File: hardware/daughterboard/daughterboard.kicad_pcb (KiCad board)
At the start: 4 copper layers, 51.1 x 51 mm, 88 parts, among them J1 Custom_PCIe_x4, U0 XTR200, U1 XTR200, U10 REF5030EIDR, U11 AD7193, U2 XTR200, U20 DAC80508Z, U3 XTR200, U4 XTR200, U5 XTR200, U6 XTR200, U7 XTR200, U8 SN74LV165

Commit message: add board
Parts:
- added FID1: Fiducial, Fiducial:Fiducial_1mm_Mask2mm, F.Cu at (101.6, 67.0)
- added FID2: Fiducial, Fiducial:Fiducial_1mm_Mask2mm, F.Cu at (149.6, 106.5)
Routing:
- net GND: vias 188 -> 193
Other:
- board text added: "KOI 8X8"
- board text removed: "OQ V1"

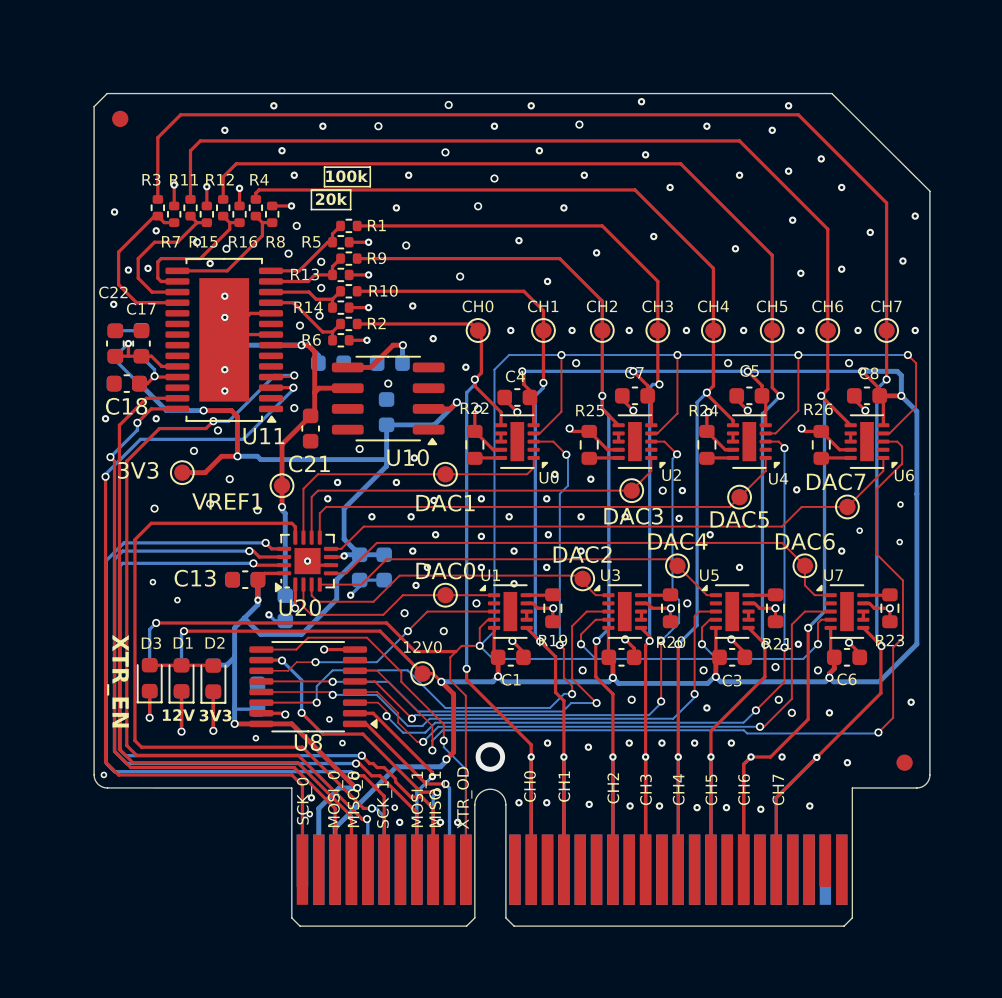
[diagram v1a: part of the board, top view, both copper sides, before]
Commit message: updated daughterboard with eeprom and some layout improvements and padne simulations
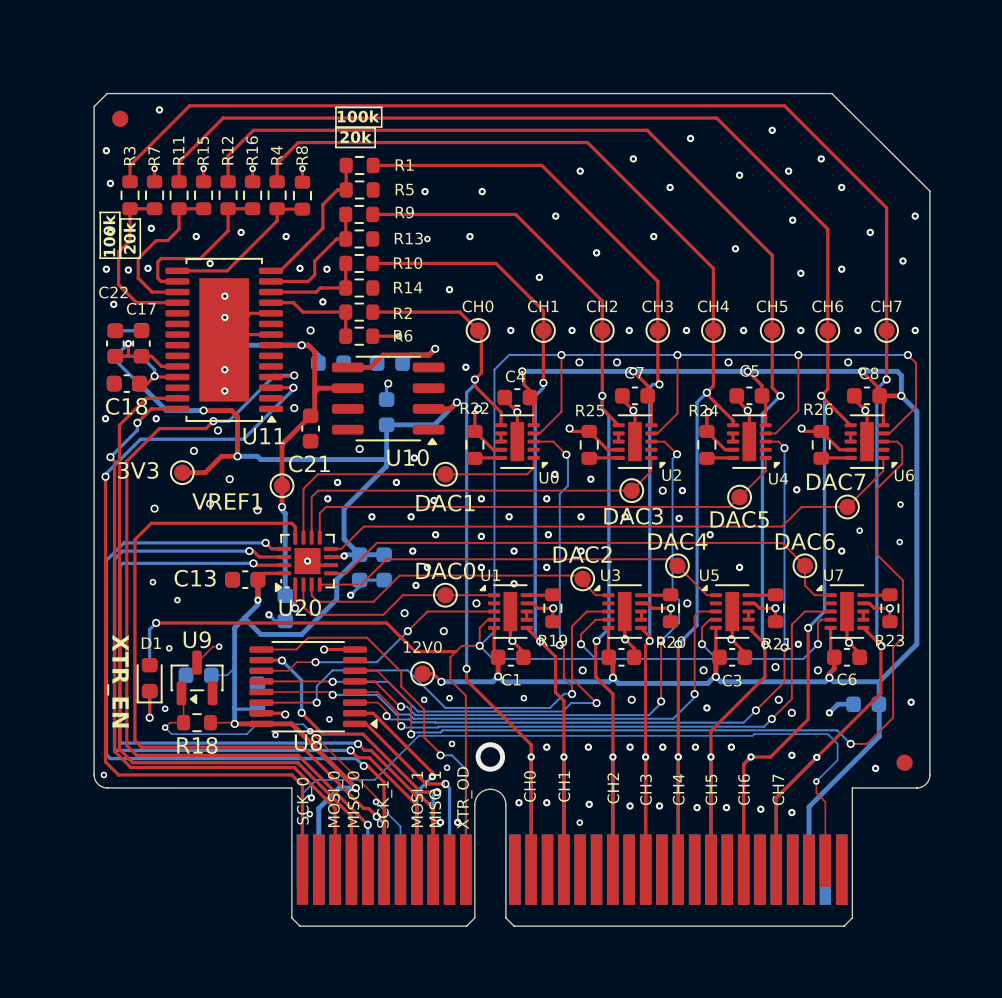
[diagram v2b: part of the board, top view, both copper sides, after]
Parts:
- removed the D1 at (105.3, 101.3)
- removed D2: LED, LED_SMD:LED_0603_1608Metric
- removed R28, R29: 100k, Resistor_SMD:R_0603_1608Metric
- added C24: 0.1uF, Capacitor_SMD:C_0603_1608Metric, B.Cu at (106.4, 101.1)
- added C25: 10uF, Capacitor_SMD:C_0603_1608Metric, B.Cu at (147.2, 102.9)
- added R18: 2.7k, Resistor_SMD:R_0603_1608Metric, F.Cu at (106.3, 104.0)
- added U9: AT21CS01, Package_TO_SOT_SMD:SOT-23, F.Cu at (106.3, 101.3)
- R1, R10, R11, R12, R13, R14, R15, R16, R2, R3, R4, R5, R6, R7, R8, R9: footprint Resistor_SMD:R_0402_1005Metric -> Resistor_SMD:R_0603_1608Metric
- moved R1 3.76 mm to (116.2, 69.9)
- moved R5 3.40 mm to (116.2, 71.4)
- moved R9 2.77 mm to (116.2, 72.9)
- moved R13 2.47 mm to (116.2, 74.4)
- moved R8 2.17 mm to (112.8, 71.8)
- moved R3 1.86 mm to (102.2, 71.7)
- moved R10 1.81 mm to (116.2, 75.9)
- moved R7 1.67 mm to (103.7, 71.7)
- moved R14 1.64 mm to (116.2, 77.4)
- moved R4 1.51 mm to (111.2, 71.7)
- moved R16 1.41 mm to (109.7, 71.7)
- moved R15 1.18 mm to (106.7, 71.7)
- moved R6 1.15 mm to (116.2, 80.3)
- moved R11 1.04 mm to (105.2, 71.7)
- moved R2 0.96 mm to (116.2, 78.9)
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- renumbered D3 to D1
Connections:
- J1 pad A1: GND -> PRSNT
- J1 pad A3: +12V -> GND
- J1 pad A30: unconnected-(J1-RSVD-PadA30) -> +12V
- J1 pad A7: GND -> AT
- J1 pad B31: GND -> PRSNT
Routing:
- net PRSNT: track 0.00 -> 46.5 mm, vias 0 -> 1
- net AT: track 0.00 -> 23.4 mm, vias 0 -> 3
- net +12V: track 135.7 -> 114.8 mm, vias 12 -> 10
- net GND: track 63.3 -> 76.4 mm, vias 193 -> 182
- net Net-(D1-K) (its old number): track 4.91 -> 0.00 mm, vias 1 -> 0
- net Net-(D2-K): track 4.79 -> 0.00 mm, vias 1 -> 0
- net CH3_V: track 5.69 -> 9.00 mm
- net Net-(U10-Trim/NR): track 5.05 -> 8.18 mm
- net CH2_V: track 5.13 -> 7.65 mm
- net CH4_V: track 8.06 -> 9.67 mm
- net +3.3V: track 91.3 -> 92.7 mm
- net CH5_V: track 9.08 -> 10.2 mm
- net CH5: track 85.7 -> 86.8 mm
- net CH4: track 77.7 -> 78.8 mm
- net CH1_V: track 5.15 -> 6.18 mm
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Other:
- board text added: "AT"
